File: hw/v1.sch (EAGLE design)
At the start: 18 parts, among them J1 FFC2B28-24-G, Q1 SI1308EDL-T1-GE3, U1 ESP32-C3-WROOM-02-H4

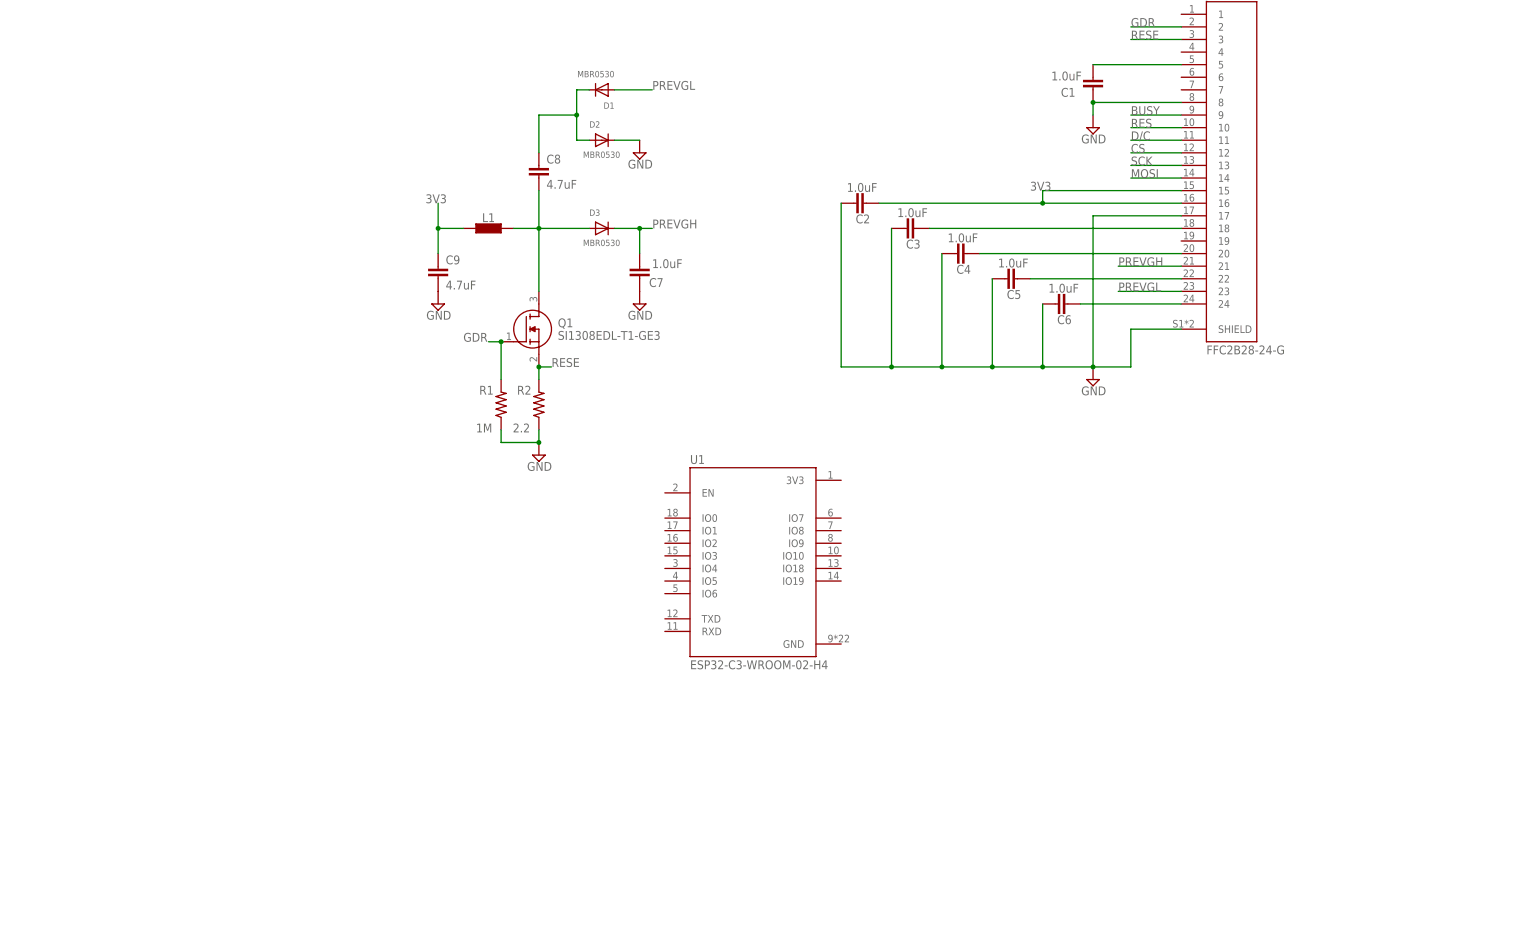
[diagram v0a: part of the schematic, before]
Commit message: Add boot buttons, rtc, ldo
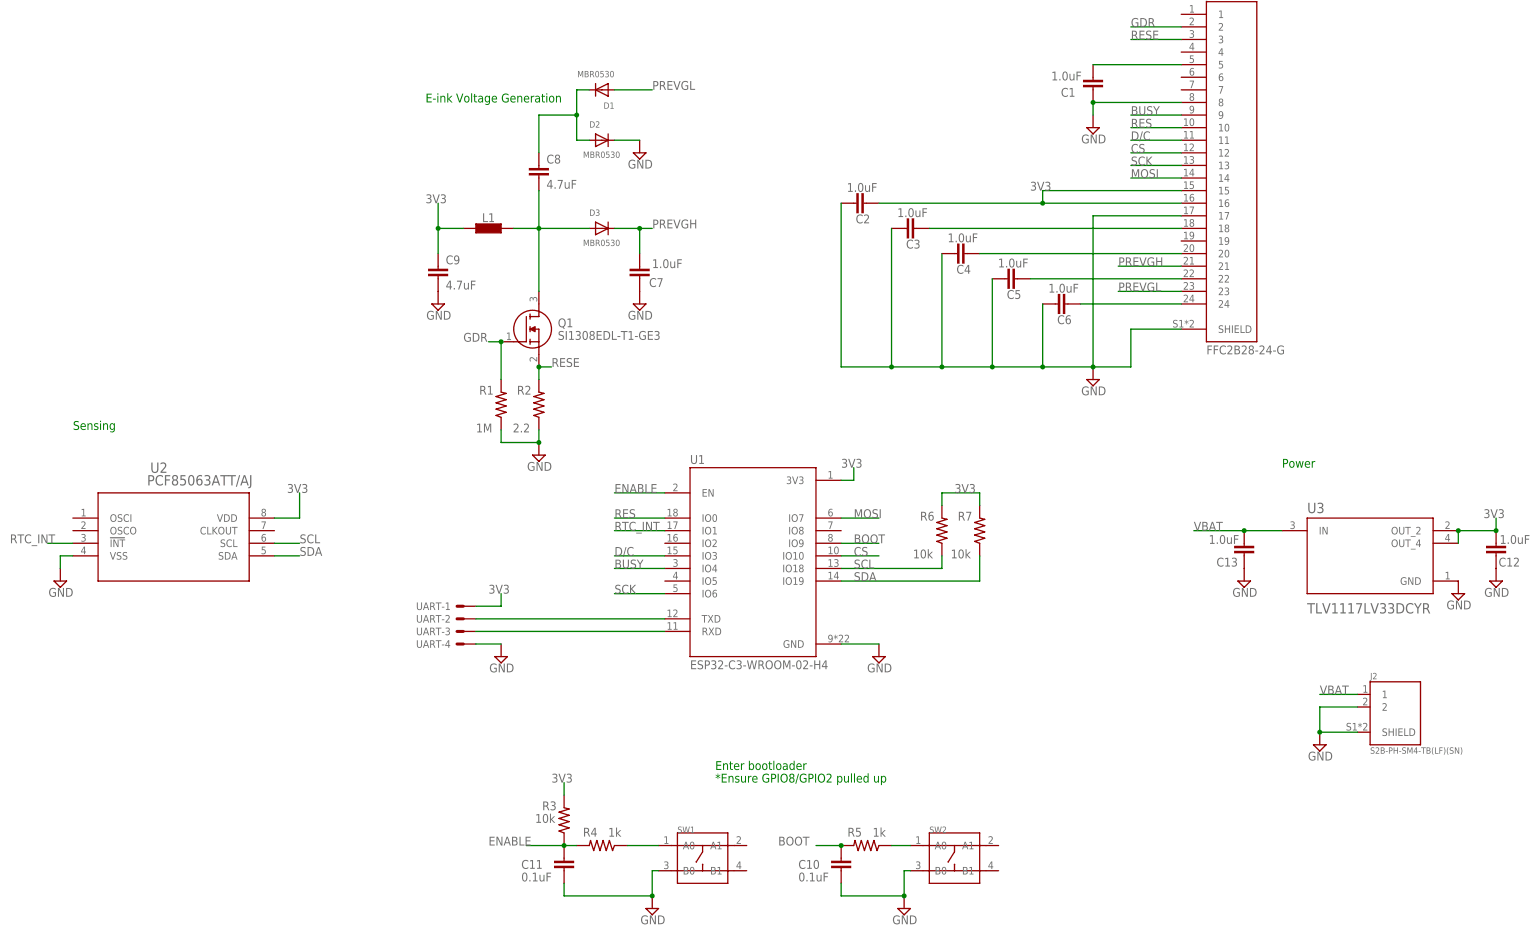
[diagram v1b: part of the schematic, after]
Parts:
- added C10, C11: 0.1uF, SparkFun-Capacitors:0.1UF-0603-25V-(+80/-20%)
- added C12, C13: 1.0uF, SparkFun-Capacitors:1.0UF-0603-16V-10%-X7R-WE
- added J2: S2B-PH-SM4-TB(LF)(SN), S2B-PH-SM4-TB_LF__SN_:S2B-PH-SM4-TB(LF)(SN)
- added R3, R6, R7: 10k, rcl:R-US_R0603
- added R4, R5: 1k, rcl:R-US_R0603
- added SW1, SW2: SMD-BUTTON(4P-5.2X5.2X1.5MM-SKQGADE010)-SKQGADE010, SMD-BUTTON_4P-5.2X5.2X1.5MM-SKQGADE010_:SMD-BUTTON(4P-5.2X5.2X1.5MM-SKQGADE010)-SKQGADE010
- added U2: PCF85063ATT/AJ, PCF85063ATT:AJ:PCF85063ATT/AJ
- added U3: TLV1117LV33DCYR, TLV1117LV33DCYR:TLV1117LV33DCYR
- added UART: 22-23-2041, con-molex:22-23-2041
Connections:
- new net BOOT: C10.1, R5.2, U1.IO9
- new net ENABLE: C11.1, R3.1, R4.2, U1.EN
- new net N$11: U1.TXD, UART-2.S
- new net N$12: U1.RXD, UART-3.S
- new net N$8: R4.1, SW1.A0
- new net N$9: R5.1, SW2.A0
- new net RTC_INT: U1.IO1, U2.!INT
- new net SCL: R6.1, U1.IO18, U2.SCL
- new net SDA: R7.1, U1.IO19, U2.SDA
- new net VBAT: C13.1, J2.1, U3.IN
- net 3V3: now also C12.1, R3.2, R6.2, R7.2, U1.3V3, U2.VDD, U3.OUT_2, U3.OUT_4, UART-1.S
- net BUSY: now also U1.IO4
- net CS: now also U1.IO10
- net D/C: now also U1.IO3
- net GND: now also C10.2, C11.2, C12.2, C13.2, J2.2, J2.SHIELD, SW1.B0, SW2.B0, U1.GND, U2.VSS, U3.GND, UART-4.S
- net MOSI: now also U1.IO7
- net RES: now also U1.IO0
- net SCK: now also U1.IO6
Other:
- note added: "*Ensure GPIO8/GPIO2 pulled up"
- note added: "E-ink Voltage Generation"
- note added: "Enter bootloader"
- note added: "Power"
- note added: "Sensing"

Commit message: Add charging hardware, change buttons
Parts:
- removed SW2: SMD-BUTTON(4P-5.2X5.2X1.5MM-SKQGADE010)-SKQGADE010, SMD-BUTTON_4P-5.2X5.2X1.5MM-SKQGADE010_:SMD-BUTTON(4P-5.2X5.2X1.5MM-SKQGADE010)-SKQGADE010
- added C14, C15: 4.7uF, SparkFun-Capacitors:4.7UF-0603-35V-(20%)
- added C16: 0.1uF, SparkFun-Capacitors:0.1UF-0603-25V-(+80/-20%)
- added J3: 10118193-0001LF, 10118193-0001LF:10118193-0001LF
- added LED1: (no value), led:LEDCHIP-LED0603
- added R10: 1k, rcl:R-US_R0603
- added R8: 470, rcl:R-US_R0603
- added R9: 2k, rcl:R-US_R0603
- added S1, S2: EVQ-P7A01P, EVQ-P7A01P:EVQ-P7A01P
- added U$1: MCP73831T-2ACI/OT, MCP73831T-2ACI_OT:MCP73831T-2ACI/OT
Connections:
- net BOOT renamed BTN2
- new net BTN1: C16.1, R10.2, U1.IO8
- new net N$10: R10.1, S2.1
- new net N$13: LED1.C, R8.2
- new net N$14: R8.1, U$1.STAT
- new net N$15: R9.1, U$1.PROG
- new net VUSB: C14.1, J3.VUSB, LED1.A, U$1.VDD
- net GND: now also C14.2, C15.2, C16.2, J3.GND, J3.SHIELD, R9.2, S1.2, S2.2, U$1.VSS; no longer SW2.B0
- net N$9: now also S1.1; no longer SW2.A0
- net VBAT: now also C15.1, U$1.VBAT
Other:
- note added: "BTN2 used for boot"
- note added: "E-ink Display"
- note added: "MCU"
- moved on the sheet: C10, C11, R3, R4, R5, SW1

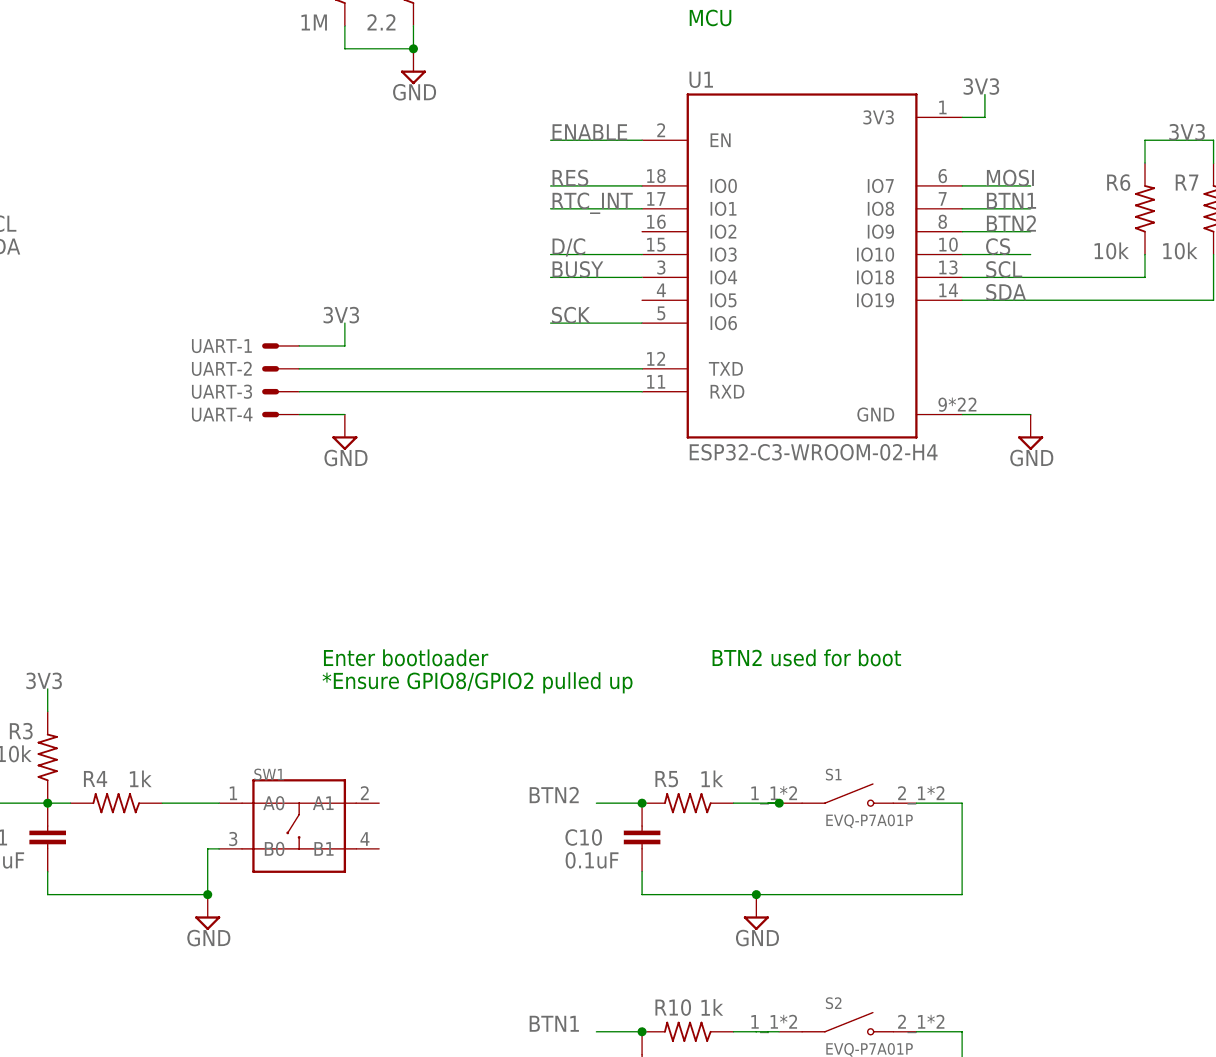
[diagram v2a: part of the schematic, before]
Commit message: Finish basic board layout, change reset button
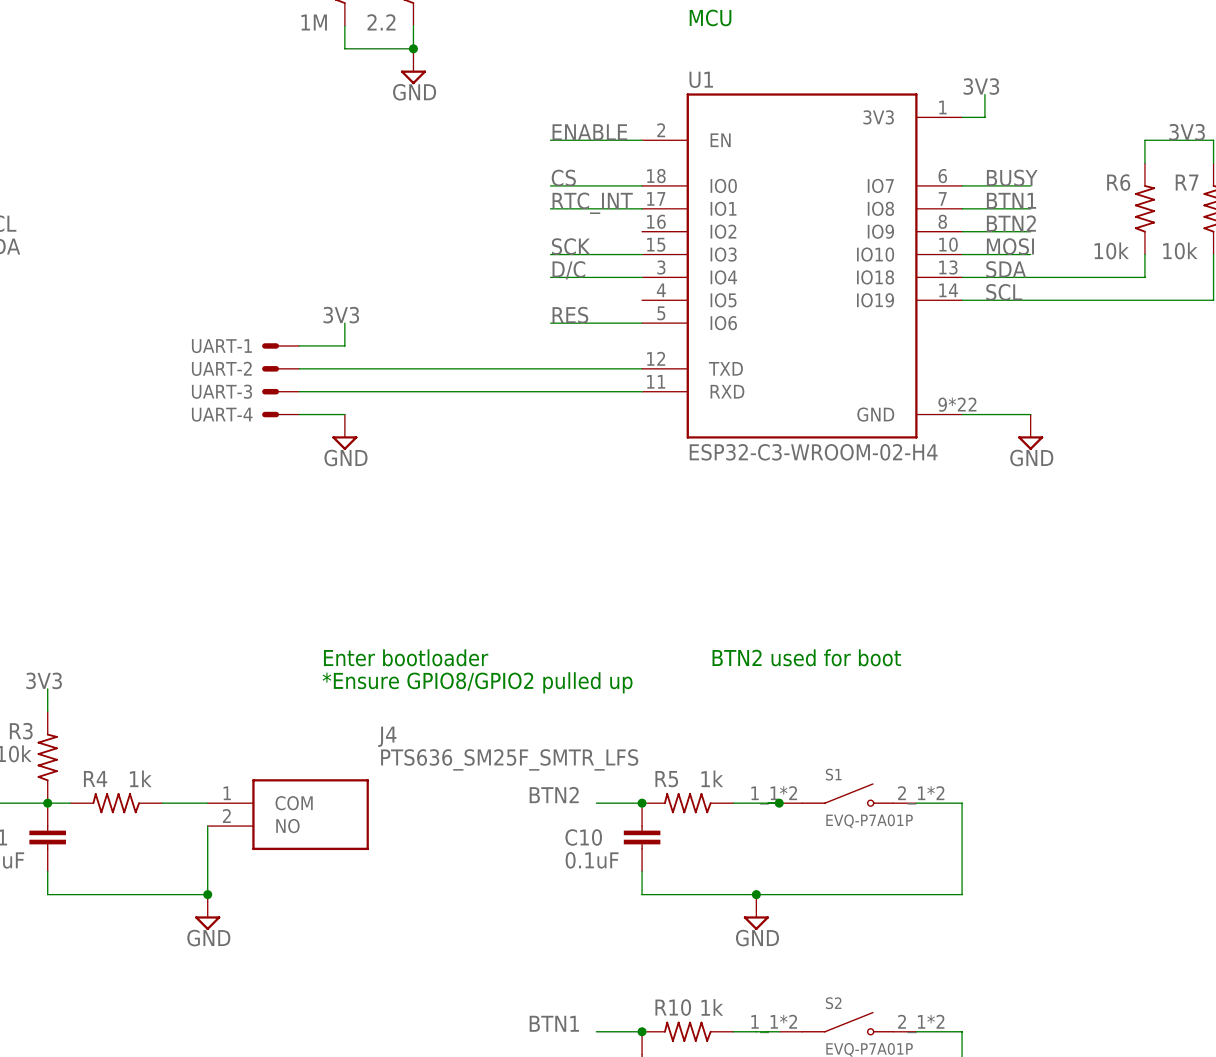
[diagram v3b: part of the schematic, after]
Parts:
- removed SW1: SMD-BUTTON(4P-5.2X5.2X1.5MM-SKQGADE010)-SKQGADE010, SMD-BUTTON_4P-5.2X5.2X1.5MM-SKQGADE010_:SMD-BUTTON(4P-5.2X5.2X1.5MM-SKQGADE010)-SKQGADE010
- added J4: PTS636_SM25F_SMTR_LFS, PTS636_SM25F_SMTR_LFS:PTS636_SM25F_SMTR_LFS
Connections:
- net BUSY: now also U1.IO7; no longer U1.IO4
- net CS: now also U1.IO0; no longer U1.IO10
- net D/C: now also U1.IO4; no longer U1.IO3
- net GND: now also J4.NO; no longer SW1.B0
- net MOSI: now also U1.IO10; no longer U1.IO7
- net N$8: now also J4.COM; no longer SW1.A0
- net RES: now also U1.IO6; no longer U1.IO0
- net SCK: now also U1.IO3; no longer U1.IO6
- net SCL: now also R7.1, U1.IO19; no longer R6.1, U1.IO18
- net SDA: now also R6.1, U1.IO18; no longer R7.1, U1.IO19
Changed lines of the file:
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@@
 <part name="R1" library="rcl" library_urn="urn:adsk.eagle:library:334" deviceset="R-US_" device="R0603" package3d_urn="urn:adsk.eagle:package:23555/3" value="1M"/>
 <part name="R2" library="rcl" library_urn="urn:adsk.eagle:library:334" deviceset="R-US_" device="R0603" package3d_urn="urn:adsk.eagle:package:23555/3" value="2.2"/>
-<part name="SW1" library="SMD-BUTTON_4P-5.2X5.2X1.5MM-SKQGADE010_" deviceset="SMD-BUTTON(4P-5.2X5.2X1.5MM-SKQGADE010)" device="-SKQGADE010"/>
 <part name="R3" library="rcl" library_urn="urn:adsk.eagle:library:334" deviceset="R-US_" device="R0603" package3d_urn="urn:adsk.eagle:package:23555/3" value="10k"/>
 <part name="SUPPLY7" library="Tutorial - Fusion 360" library_urn="urn:adsk.eagle:library:16997205" deviceset="GND" device="" value="GND"/>
@@
 <part name="S1" library="EVQ-P7A01P" deviceset="EVQ-P7A01P" device=""/>
 <part name="S2" library="EVQ-P7A01P" deviceset="EVQ-P7A01P" device=""/>
+<part name="J4" library="PTS636_SM25F_SMTR_LFS" deviceset="PTS636_SM25F_SMTR_LFS" device=""/>
 </parts>
 <sheets>
@@
 <attribute name="VALUE" x="-44.958" y="29.21" size="1.778" layer="96" rot="R180"/>
 </instance>
-<instance part="SW1" gate="G$1" x="-55.88" y="-60.96" smashed="yes">
-<attribute name="NAME" x="-60.965890625" y="-55.874109375" size="1.27146875" layer="95" ratio="10"/>
-</instance>
 <instance part="R3" gate="G$1" x="-83.82" y="-53.34" smashed="yes" rot="R90">
 <attribute name="NAME" x="-85.3186" y="-49.53" size="1.778" layer="95" rot="R180"/>
@@
 <attribute name="NAME" x="2.54" y="-81.28" size="1.27" layer="95"/>
 <attribute name="VALUE" x="2.54" y="-86.36" size="1.27" layer="96"/>
+</instance>
+<instance part="J4" gate="G$1" x="-66.04" y="-58.42" smashed="yes">
+<attribute name="NAME" x="-46.99" y="-50.8" size="1.778" layer="95" align="center-left"/>
+<attribute name="VALUE" x="-46.99" y="-53.34" size="1.778" layer="96" align="center-left"/>
 </instance>
 </instances>
@@
 </segment>
 <segment>
+<pinref part="U1" gate="G$1" pin="IO7"/>
+<wire x1="17.78" y1="10.16" x2="25.4" y2="10.16" width="0.1524" layer="91"/>
+<label x="20.32" y="10.16" size="1.778" layer="95"/>
+</segment>
+</net>
+<net name="RES" class="0">
+<segment>
+<pinref part="J1" gate="G$1" pin="10"/>
+<wire x1="86.36" y1="88.9" x2="76.2" y2="88.9" width="0.1524" layer="91"/>
+<label x="76.2" y="88.9" size="1.778" layer="95"/>
+</segment>
+<segment>
+<pinref part="U1" gate="G$1" pin="IO6"/>
+<wire x1="-17.78" y1="-5.08" x2="-27.94" y2="-5.08" width="0.1524" layer="91"/>
+<label x="-27.94" y="-5.08" size="1.778" layer="95"/>
+</segment>
+</net>
+<net name="D/C" class="0">
+<segment>
+<pinref part="J1" gate="G$1" pin="11"/>
+<wire x1="86.36" y1="86.36" x2="76.2" y2="86.36" width="0.1524" layer="91"/>
+<label x="76.2" y="86.36" size="1.778" layer="95"/>
+</segment>
+<segment>
 <pinref part="U1" gate="G$1" pin="IO4"/>
 <wire x1="-17.78" y1="0" x2="-27.94" y2="0" width="0.1524" layer="91"/>
@@
 </segment>
 </net>
-<net name="RES" class="0">
-<segment>
-<pinref part="J1" gate="G$1" pin="10"/>
-<wire x1="86.36" y1="88.9" x2="76.2" y2="88.9" width="0.1524" layer="91"/>
-<label x="76.2" y="88.9" size="1.778" layer="95"/>
+<net name="CS" class="0">
+<segment>
+<pinref part="J1" gate="G$1" pin="12"/>
+<wire x1="86.36" y1="83.82" x2="76.2" y2="83.82" width="0.1524" layer="91"/>
+<label x="76.2" y="83.82" size="1.778" layer="95"/>
 </segment>
 <segment>
@@
 </segment>
 </net>
-<net name="D/C" class="0">
-<segment>
-<pinref part="J1" gate="G$1" pin="11"/>
-<wire x1="86.36" y1="86.36" x2="76.2" y2="86.36" width="0.1524" layer="91"/>
-<label x="76.2" y="86.36" size="1.778" layer="95"/>
+<net name="SCK" class="0">
+<segment>
+<pinref part="J1" gate="G$1" pin="13"/>
+<wire x1="86.36" y1="81.28" x2="76.2" y2="81.28" width="0.1524" layer="91"/>
+<label x="76.2" y="81.28" size="1.778" layer="95"/>
 </segment>
 <segment>
@@
 </segment>
 </net>
-<net name="CS" class="0">
-<segment>
-<pinref part="J1" gate="G$1" pin="12"/>
-<wire x1="86.36" y1="83.82" x2="76.2" y2="83.82" width="0.1524" layer="91"/>
-<label x="76.2" y="83.82" size="1.778" layer="95"/>
+<net name="MOSI" class="0">
+<segment>
+<pinref part="J1" gate="G$1" pin="14"/>
+<wire x1="86.36" y1="78.74" x2="76.2" y2="78.74" width="0.1524" layer="91"/>
+<label x="76.2" y="78.74" size="1.778" layer="95"/>
 </segment>
 <segment>
@@
 <wire x1="17.78" y1="2.54" x2="25.4" y2="2.54" width="0.1524" layer="91"/>
 <label x="20.32" y="2.54" size="1.778" layer="95"/>
-</segment>
-</net>
-<net name="SCK" class="0">
-<segment>
-<pinref part="J1" gate="G$1" pin="13"/>
-<wire x1="86.36" y1="81.28" x2="76.2" y2="81.28" width="0.1524" layer="91"/>
-<label x="76.2" y="81.28" size="1.778" layer="95"/>
-</segment>
-<segment>
-<pinref part="U1" gate="G$1" pin="IO6"/>
-<wire x1="-17.78" y1="-5.08" x2="-27.94" y2="-5.08" width="0.1524" layer="91"/>
-<label x="-27.94" y="-5.08" size="1.778" layer="95"/>
-</segment>
-</net>
-<net name="MOSI" class="0">
-<segment>
-<pinref part="J1" gate="G$1" pin="14"/>
-<wire x1="86.36" y1="78.74" x2="76.2" y2="78.74" width="0.1524" layer="91"/>
-<label x="76.2" y="78.74" size="1.778" layer="95"/>
-</segment>
-<segment>
-<pinref part="U1" gate="G$1" pin="IO7"/>
-<wire x1="17.78" y1="10.16" x2="25.4" y2="10.16" width="0.1524" layer="91"/>
-<label x="20.32" y="10.16" size="1.778" layer="95"/>
 </segment>
 </net>
@@
 </segment>
 <segment>
-<pinref part="SW1" gate="G$1" pin="B0"/>
-<wire x1="-64.77" y1="-63.5" x2="-66.04" y2="-63.5" width="0.1524" layer="91"/>
-<wire x1="-66.04" y1="-63.5" x2="-66.04" y2="-68.58" width="0.1524" layer="91"/>
 <pinref part="SUPPLY7" gate="G$1" pin="GND"/>
 <wire x1="-83.82" y1="-66.04" x2="-83.82" y2="-68.58" width="0.1524" layer="91"/>
 <wire x1="-83.82" y1="-68.58" x2="-66.04" y2="-68.58" width="0.1524" layer="91"/>
+<pinref part="C11" gate="G$1" pin="2"/>
 <junction x="-66.04" y="-68.58"/>
-<pinref part="C11" gate="G$1" pin="2"/>
+<pinref part="J4" gate="G$1" pin="NO"/>
+<wire x1="-66.04" y1="-60.96" x2="-66.04" y2="-68.58" width="0.1524" layer="91"/>
 </segment>
 <segment>
@@
 </segment>
 </net>
-<net name="N$8" class="0">
-<segment>
-<pinref part="SW1" gate="G$1" pin="A0"/>
-<wire x1="-64.77" y1="-58.42" x2="-71.12" y2="-58.42" width="0.1524" layer="91"/>
-<pinref part="R4" gate="G$1" pin="1"/>
-</segment>
-</net>
 <net name="N$9" class="0">
 <segment>
@@
 </segment>
 <segment>
+<pinref part="U1" gate="G$1" pin="IO18"/>
+<label x="20.32" y="0" size="1.778" layer="95"/>
+<wire x1="17.78" y1="0" x2="38.1" y2="0" width="0.1524" layer="91"/>
+<wire x1="38.1" y1="0" x2="38.1" y2="2.54" width="0.1524" layer="91"/>
+<pinref part="R6" gate="G$1" pin="1"/>
+</segment>
+</net>
+<net name="SCL" class="0">
+<segment>
+<pinref part="U2" gate="A" pin="SCL"/>
+<wire x1="-96.52" y1="5.08" x2="-91.44" y2="5.08" width="0.1524" layer="91"/>
+<label x="-91.44" y="5.08" size="1.778" layer="95"/>
+</segment>
+<segment>
 <pinref part="U1" gate="G$1" pin="IO19"/>
 <label x="20.32" y="-2.54" size="1.778" layer="95"/>
@@
 <wire x1="45.72" y1="-2.54" x2="45.72" y2="2.54" width="0.1524" layer="91"/>
 <pinref part="R7" gate="G$1" pin="1"/>
-</segment>
-</net>
-<net name="SCL" class="0">
-<segment>
-<pinref part="U1" gate="G$1" pin="IO18"/>
-<label x="20.32" y="0" size="1.778" layer="95"/>
-<wire x1="17.78" y1="0" x2="38.1" y2="0" width="0.1524" layer="91"/>
-<wire x1="38.1" y1="0" x2="38.1" y2="2.54" width="0.1524" layer="91"/>
-<pinref part="R6" gate="G$1" pin="1"/>
-</segment>
-<segment>
-<pinref part="U2" gate="A" pin="SCL"/>
-<wire x1="-96.52" y1="5.08" x2="-91.44" y2="5.08" width="0.1524" layer="91"/>
-<label x="-91.44" y="5.08" size="1.778" layer="95"/>
 </segment>
 </net>
@@
 </segment>
 </net>
+<net name="N$8" class="0">
+<segment>
+<pinref part="R4" gate="G$1" pin="1"/>
+<pinref part="J4" gate="G$1" pin="COM"/>
+<wire x1="-71.12" y1="-58.42" x2="-66.04" y2="-58.42" width="0.1524" layer="91"/>
+</segment>
+</net>
